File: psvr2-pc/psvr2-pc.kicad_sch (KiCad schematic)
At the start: 89 parts, among them IC1 SN65MLVD200D, IC2 SN65MLVD200D, J1 USB_C_Receptacle, J2 USB3_B_Micro, J3 DP_47272, J4 Barrel_Jack_Switch, J5 Conn_01x02_Pin, Q1 IRF4905, Q2 PN2222A, Q3 IRF9530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

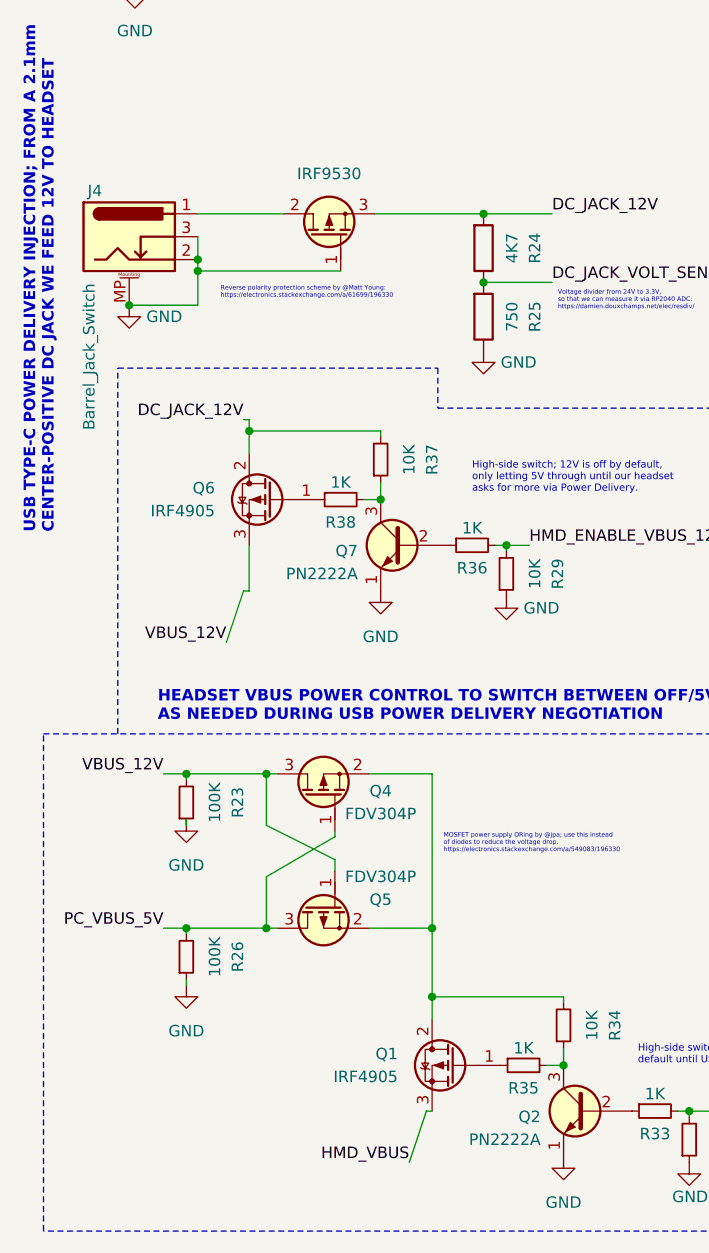
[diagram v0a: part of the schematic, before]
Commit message: Change all the P MOSFETs to Si2301CDS_1_1, and use the correct SOT-23 footprint.
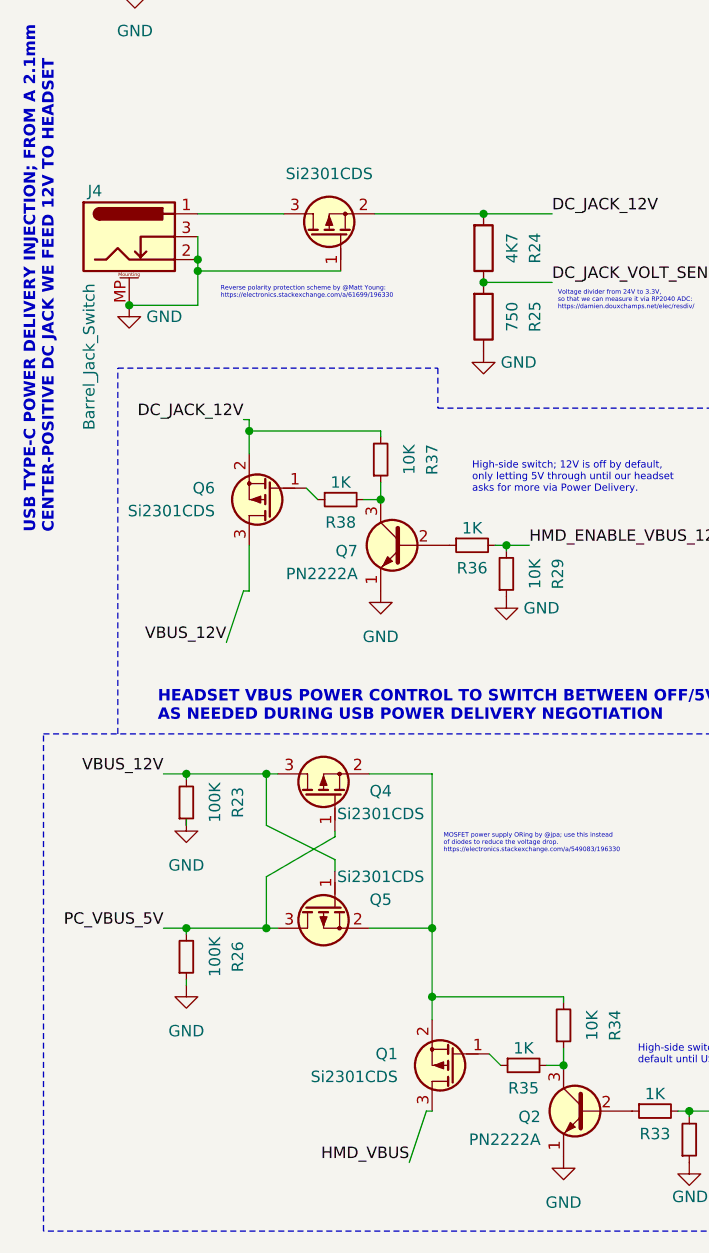
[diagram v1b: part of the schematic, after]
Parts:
- Q1, Q6: value IRF4905 -> Si2301CDS; footprint Package_TO_SOT_SMD:SOT-223 -> Package_TO_SOT_SMD:SOT-23; symbol Transistor_FET:IRF4905 -> PCM_Transistor_MOSFET_AKL:Si2301CDS
- Q2, Q7: footprint Package_TO_SOT_SMD:SOT-223 -> Package_TO_SOT_SMD:SOT-23
- Q3: value IRF9530 -> Si2301CDS; footprint Package_TO_SOT_SMD:SOT-223 -> Package_TO_SOT_SMD:SOT-23; symbol PCM_Transistor_MOSFET_AKL:IRF9530 -> PCM_Transistor_MOSFET_AKL:Si2301CDS
- Q4, Q5: value FDV304P -> Si2301CDS; footprint Package_TO_SOT_SMD:SOT-223 -> Package_TO_SOT_SMD:SOT-23; symbol PCM_Transistor_MOSFET_AKL:FDV304P -> PCM_Transistor_MOSFET_AKL:Si2301CDS
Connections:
- net DC_JACK_12V: now also Q3.2 (S); no longer Q3.3 (S)
- net at J4.1: now also Q3.3 (D); no longer Q3.2 (D)
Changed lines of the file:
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@@
     (stroke (width 0) (type default))
   )
+  (wire (pts (xy 66.04 233.045) (xy 64.77 231.775))
+    (stroke (width 0) (type default))
+  )
   (wire (pts (xy 41.91 33.02) (xy 43.18 33.02))
     (stroke (width 0) (type default))
@@
     (stroke (width 0) (type default))
   )
+  (wire (pts (xy 44.45 168.91) (xy 45.72 170.18))
+    (stroke (width 0) (type default))
+  )
   (wire (pts (xy 194.31 217.17) (xy 192.405 219.075))
     (stroke (width 0) (type default))
@@
     )
   )
-  (symbol (lib_id "PCM_Transistor_MOSFET_AKL:FDV304P") (at 46.355 203.2 270) (mirror x) (unit 1)
+  (symbol (lib_id "PCM_Transistor_MOSFET_AKL:Si2301CDS") (at 46.355 203.2 270) (mirror x) (unit 1)
     (in_bom yes) (on_board yes) (dnp no)
     (property "Reference" "Q4" (at 52.705 202.565 90)
       (effects (font (size 1.27 1.27)))
     )
-    (property "Value" "FDV304P" (at 52.705 205.105 90)
+    (property "Value" "Si2301CDS" (at 52.705 205.105 90)
       (effects (font (size 1.27 1.27)))
     )
-    (property "Footprint" "Package_TO_SOT_SMD:SOT-223" (at 43.815 198.12 0)
+    (property "Footprint" "Package_TO_SOT_SMD:SOT-23" (at 43.815 198.12 0)
       (effects (font (size 1.27 1.27)) hide)
     )
-    (property "Datasheet" "https://www.tme.eu/Document/ac19ef9dcb7c8350177895b6b37394d9/FDV304P.pdf" (at 46.355 203.2 0)
+    (property "Datasheet" "https://www.tme.eu/Document/519498819e90b407235adccdceba4014/SI2301CDS-T1-GE3.pdf" (at 46.355 203.2 0)
       (effects (font (size 1.27 1.27)) hide)
     )
@@
     )
   )
-  (symbol (lib_id "Transistor_FET:IRF4905") (at 60.96 233.045 0) (mirror y) (unit 1)
+  (symbol (lib_id "PCM_Transistor_MOSFET_AKL:Si2301CDS") (at 60.96 233.045 0) (mirror y) (unit 1)
     (in_bom yes) (on_board yes) (dnp no) (fields_autoplaced)
     (property "Reference" "Q1" (at 54.61 231.775 0)
       (effects (font (size 1.27 1.27)) (justify left))
     )
-    (property "Value" "IRF4905" (at 54.61 234.315 0)
+    (property "Value" "Si2301CDS" (at 54.61 234.315 0)
       (effects (font (size 1.27 1.27)) (justify left))
     )
-    (property "Footprint" "Package_TO_SOT_SMD:SOT-223" (at 55.88 234.95 0)
-      (effects (font (size 1.27 1.27) italic) (justify left) hide)
+    (property "Footprint" "Package_TO_SOT_SMD:SOT-23" (at 55.88 235.585 0)
+      (effects (font (size 1.27 1.27)) hide)
     )
-    (property "Datasheet" "http://www.infineon.com/dgdl/irf4905.pdf?fileId=5546d462533600a4015355e32165197c" (at 55.88 236.855 0)
-      (effects (font (size 1.27 1.27)) (justify left) hide)
+    (property "Datasheet" "https://www.tme.eu/Document/519498819e90b407235adccdceba4014/SI2301CDS-T1-GE3.pdf" (at 60.96 233.045 0)
+      (effects (font (size 1.27 1.27)) hide)
     )
     (pin "2")
@@
     )
   )
-  (symbol (lib_id "PCM_Transistor_MOSFET_AKL:IRF9530") (at 46.99 140.97 270) (mirror x) (unit 1)
+  (symbol (lib_id "PCM_Transistor_MOSFET_AKL:Si2301CDS") (at 46.99 140.97 270) (mirror x) (unit 1)
     (in_bom yes) (on_board yes) (dnp no)
     (property "Reference" "Q3" (at 46.99 131.445 90)
       (effects (font (size 1.27 1.27)) hide)
     )
-    (property "Value" "IRF9530" (at 46.99 133.985 90)
+    (property "Value" "Si2301CDS" (at 46.99 133.985 90)
       (effects (font (size 1.27 1.27)))
     )
-    (property "Footprint" "Package_TO_SOT_SMD:SOT-223" (at 44.45 135.89 0)
+    (property "Footprint" "Package_TO_SOT_SMD:SOT-23" (at 44.45 135.89 0)
       (effects (font (size 1.27 1.27)) hide)
     )
-    (property "Datasheet" "https://www.tme.eu/Document/335a97806515fd5b19419c5cf112a667/irf9530.pdf" (at 46.99 140.97 0)
+    (property "Datasheet" "https://www.tme.eu/Document/519498819e90b407235adccdceba4014/SI2301CDS-T1-GE3.pdf" (at 46.99 140.97 0)
       (effects (font (size 1.27 1.27)) hide)
     )
@@
       (effects (font (size 1.27 1.27)) (justify left))
     )
-    (property "Footprint" "Package_TO_SOT_SMD:SOT-223" (at 50.165 172.72 0)
+    (property "Footprint" "Package_TO_SOT_SMD:SOT-23" (at 50.165 172.72 0)
       (effects (font (size 1.27 1.27)) hide)
     )
@@
     )
   )
-  (symbol (lib_id "Transistor_FET:IRF4905") (at 40.64 170.18 0) (mirror y) (unit 1)
+  (symbol (lib_id "PCM_Transistor_MOSFET_AKL:Si2301CDS") (at 40.64 170.18 0) (mirror y) (unit 1)
     (in_bom yes) (on_board yes) (dnp no) (fields_autoplaced)
     (property "Reference" "Q6" (at 34.29 168.91 0)
       (effects (font (size 1.27 1.27)) (justify left))
     )
-    (property "Value" "IRF4905" (at 34.29 171.45 0)
+    (property "Value" "Si2301CDS" (at 34.29 171.45 0)
       (effects (font (size 1.27 1.27)) (justify left))
     )
-    (property "Footprint" "Package_TO_SOT_SMD:SOT-223" (at 35.56 172.085 0)
-      (effects (font (size 1.27 1.27) italic) (justify left) hide)
+    (property "Footprint" "Package_TO_SOT_SMD:SOT-23" (at 35.56 172.72 0)
+      (effects (font (size 1.27 1.27)) hide)
     )
-    (property "Datasheet" "http://www.infineon.com/dgdl/irf4905.pdf?fileId=5546d462533600a4015355e32165197c" (at 35.56 173.99 0)
-      (effects (font (size 1.27 1.27)) (justify left) hide)
+    (property "Datasheet" "https://www.tme.eu/Document/519498819e90b407235adccdceba4014/SI2301CDS-T1-GE3.pdf" (at 40.64 170.18 0)
+      (effects (font (size 1.27 1.27)) hide)
     )
     (pin "2")
@@
       (effects (font (size 1.27 1.27)) (justify left))
     )
-    (property "Footprint" "Package_TO_SOT_SMD:SOT-223" (at 70.485 235.585 0)
+    (property "Footprint" "Package_TO_SOT_SMD:SOT-23" (at 70.485 235.585 0)
       (effects (font (size 1.27 1.27)) hide)
     )
@@
     )
   )
-  (symbol (lib_id "PCM_Transistor_MOSFET_AKL:FDV304P") (at 46.355 215.265 270) (unit 1)
+  (symbol (lib_id "PCM_Transistor_MOSFET_AKL:Si2301CDS") (at 46.355 215.265 270) (unit 1)
     (in_bom yes) (on_board yes) (dnp no)
     (property "Reference" "Q5" (at 52.705 214.63 90)
       (effects (font (size 1.27 1.27)))
     )
-    (property "Value" "FDV304P" (at 52.705 212.09 90)
+    (property "Value" "Si2301CDS" (at 52.705 212.09 90)
       (effects (font (size 1.27 1.27)))
     )
-    (property "Footprint" "Package_TO_SOT_SMD:SOT-223" (at 43.815 220.345 0)
+    (property "Footprint" "Package_TO_SOT_SMD:SOT-23" (at 43.815 220.345 0)
       (effects (font (size 1.27 1.27)) hide)
     )
-    (property "Datasheet" "https://www.tme.eu/Document/ac19ef9dcb7c8350177895b6b37394d9/FDV304P.pdf" (at 46.355 215.265 0)
+    (property "Datasheet" "https://www.tme.eu/Document/519498819e90b407235adccdceba4014/SI2301CDS-T1-GE3.pdf" (at 46.355 215.265 0)
       (effects (font (size 1.27 1.27)) hide)
     )

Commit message: Use a more normal pinheader hole for the SWD stuff/debugging pins for the RP2040 microcontroller. Make it not part of the buyable parts/optional.
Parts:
- J5: footprint Connector:Banana_Jack_2Pin -> Connector_PinHeader_1.00mm:PinHeader_1x02_P1.00mm_Vertical; now left out of the parts list
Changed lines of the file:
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@@
   )
   (symbol (lib_id "Connector:Conn_01x02_Pin") (at 208.915 205.105 270) (mirror x) (unit 1)
-    (in_bom yes) (on_board yes) (dnp no)
+    (in_bom no) (on_board yes) (dnp no)
     (property "Reference" "J5" (at 205.74 208.915 90)
       (effects (font (size 1.27 1.27)) (justify left))
@@
       (effects (font (size 1.27 1.27)) (justify left))
     )
-    (property "Footprint" "Connector:Banana_Jack_2Pin" (at 208.915 205.105 0)
+    (property "Footprint" "Connector_PinHeader_1.00mm:PinHeader_1x02_P1.00mm_Vertical" (at 208.915 205.105 0)
       (effects (font (size 1.27 1.27)) hide)
     )

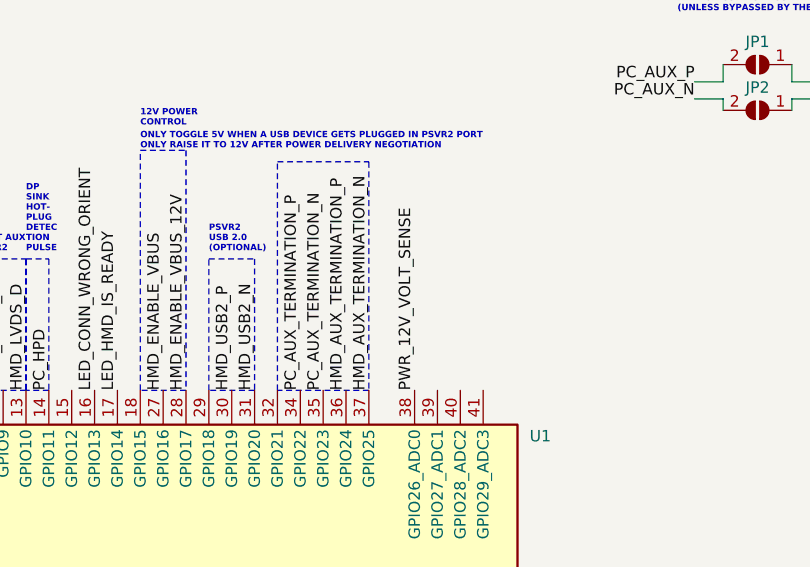
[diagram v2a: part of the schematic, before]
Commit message: Start routing things like power. And more tentative GPIO.
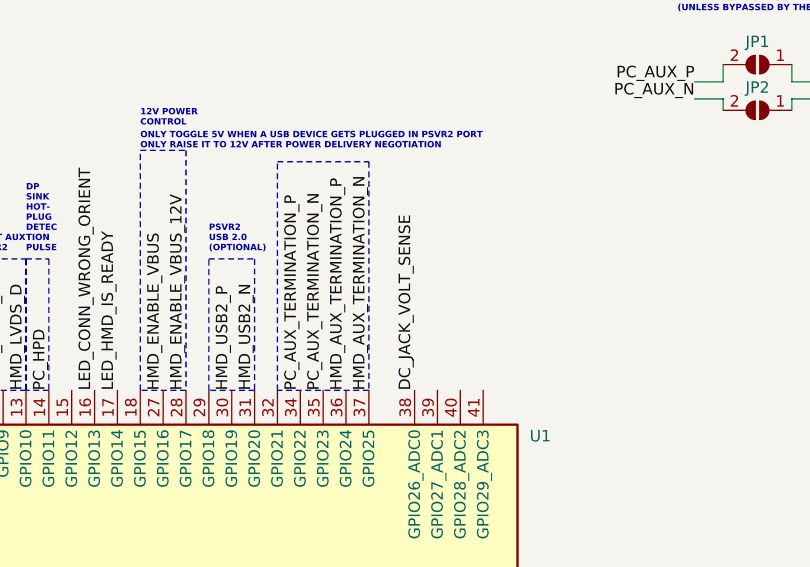
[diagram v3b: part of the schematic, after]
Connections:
- net PWR_12V_VOLT_SENSE is gone; now on net DC_JACK_VOLT_SENSE: U1.38 (GPIO26_ADC0)
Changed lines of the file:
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@@
     (effects (font (size 1.27 1.27)) (justify right bottom))
   )
-  (label "PWR_12V_VOLT_SENSE" (at 208.915 149.225 90) (fields_autoplaced)
+  (label "DC_JACK_VOLT_SENSE" (at 208.915 149.225 90) (fields_autoplaced)
     (effects (font (size 1.27 1.27)) (justify left bottom))
   )

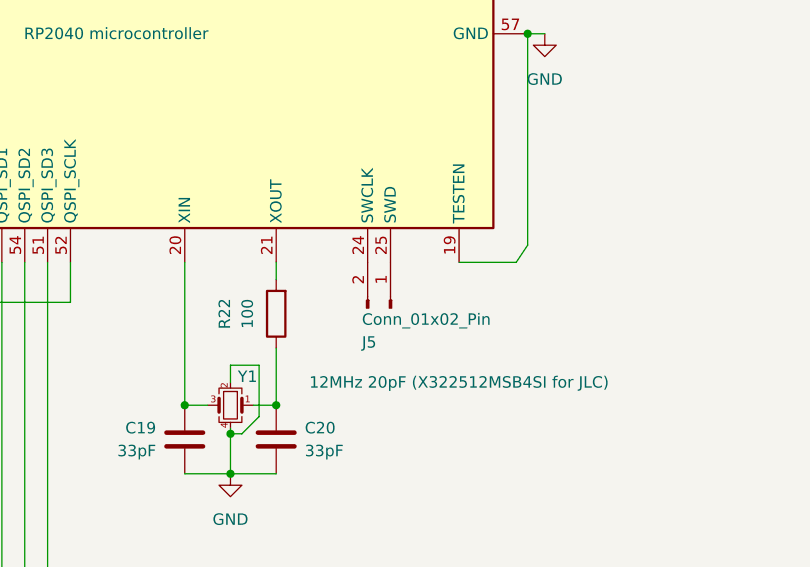
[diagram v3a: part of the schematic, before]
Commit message: Make the SWD pin header have another pin for ground. Reduce the DRC error count a bit more, add more track leeway, reduce polygon overlaps and add missing connections, mainly 3V3 power.
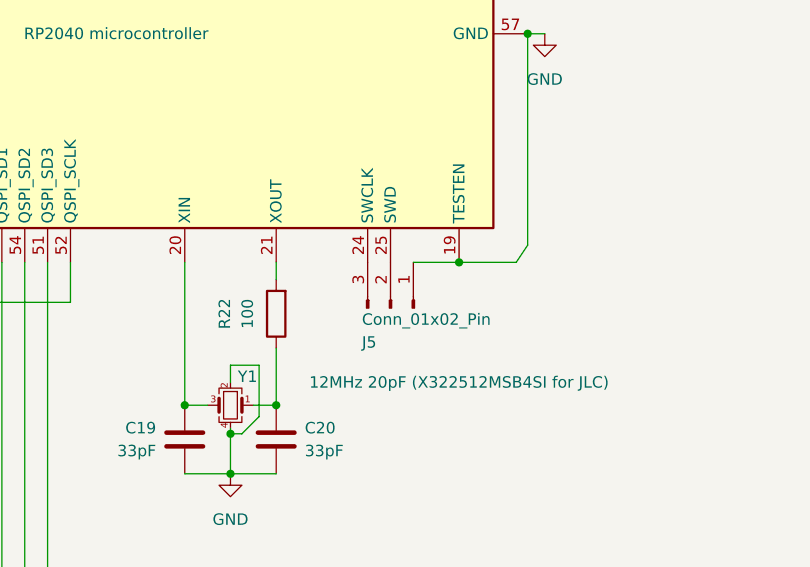
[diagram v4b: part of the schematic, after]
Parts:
- J5: footprint Connector_PinHeader_1.00mm:PinHeader_1x02_P1.00mm_Vertical -> Connector_PinHeader_1.00mm:PinHeader_1x03_P1.00mm_Vertical; symbol Connector:Conn_01x02_Pin -> Connector:Conn_01x03_Pin; now in the parts list
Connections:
- net GND: now also J5.1 (Pin_1)
- net at U1.25 (SWD): now also J5.2 (Pin_2); no longer J5.1 (Pin_1)
- net at U1.24 (SWCLK): now also J5.3 (Pin_3); no longer J5.2 (Pin_2)
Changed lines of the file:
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@@
   (junction (at 297.18 153.67) (diameter 0) (color 0 0 0 0)
   )
+  (junction (at 216.535 200.025) (diameter 0) (color 0 0 0 0)
+  )
   (junction (at 320.675 146.05) (diameter 0) (color 0 0 0 0)
   )
@@
     (stroke (width 0) (type default))
   )
+  (wire (pts (xy 211.455 200.025) (xy 216.535 200.025))
+    (stroke (width 0) (type default))
+  )
   (wire (pts (xy 374.015 23.495) (xy 377.19 23.495))
     (stroke (width 0) (type default))
@@
     )
   )
-  (symbol (lib_id "Connector:Conn_01x02_Pin") (at 208.915 205.105 270) (mirror x) (unit 1)
-    (in_bom no) (on_board yes) (dnp no)
+  (symbol (lib_id "Connector:Conn_01x03_Pin") (at 208.915 205.105 270) (mirror x) (unit 1)
+    (in_bom yes) (on_board yes) (dnp no)
     (property "Reference" "J5" (at 205.74 208.915 90)
       (effects (font (size 1.27 1.27)) (justify left))
@@
       (effects (font (size 1.27 1.27)) (justify left))
     )
-    (property "Footprint" "Connector_PinHeader_1.00mm:PinHeader_1x02_P1.00mm_Vertical" (at 208.915 205.105 0)
+    (property "Footprint" "Connector_PinHeader_1.00mm:PinHeader_1x03_P1.00mm_Vertical" (at 208.915 205.105 0)
       (effects (font (size 1.27 1.27)) hide)
     )
@@
     (pin "1")
     (pin "2")
+    (pin "3")
     (instances
       (project "psvr2-pc"

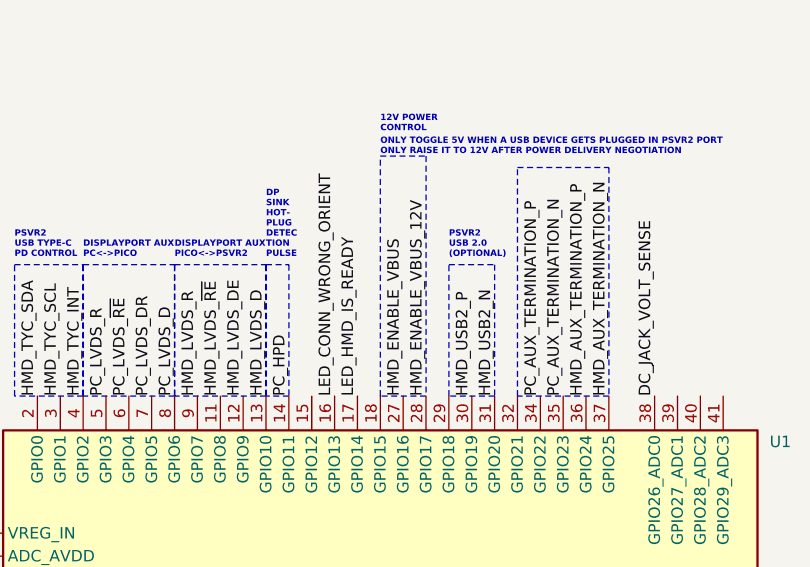
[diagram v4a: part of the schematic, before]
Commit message: Swap to GPIOs to make routing slightly less messy. Make the Open Source Hardware logo line up with the 12V track. Other extra circuiting.
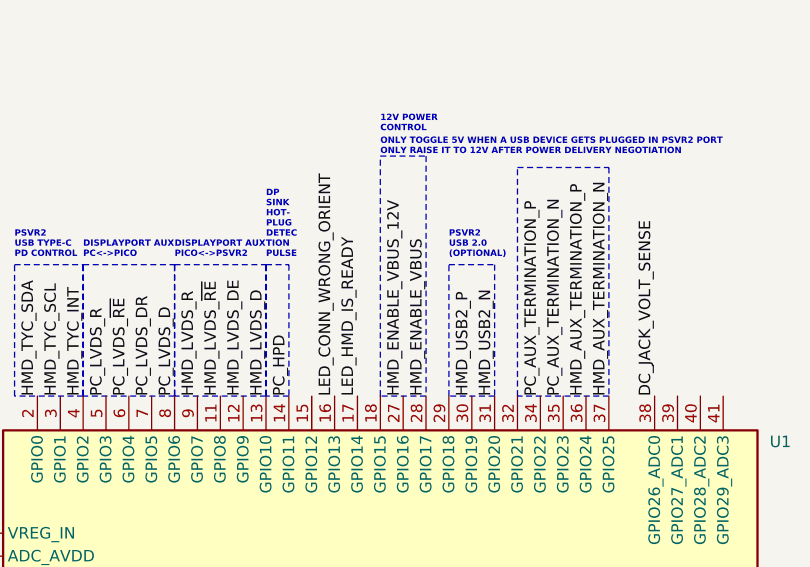
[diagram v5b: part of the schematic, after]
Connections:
- net HMD_ENABLE_VBUS: now also U1.28 (GPIO17); no longer U1.27 (GPIO16)
- net HMD_ENABLE_VBUS_12V: now also U1.27 (GPIO16); no longer U1.28 (GPIO17)
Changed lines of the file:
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@@
     (effects (font (size 1.27 1.27)) (justify right bottom))
   )
-  (label "HMD_ENABLE_VBUS_12V" (at 183.515 149.225 90) (fields_autoplaced)
+  (label "HMD_ENABLE_VBUS" (at 183.515 149.225 90) (fields_autoplaced)
     (effects (font (size 1.27 1.27)) (justify left bottom))
   )
@@
     (effects (font (size 1.27 1.27)) (justify right bottom))
   )
-  (label "HMD_ENABLE_VBUS" (at 180.975 149.225 90) (fields_autoplaced)
+  (label "HMD_ENABLE_VBUS_12V" (at 180.975 149.225 90) (fields_autoplaced)
     (effects (font (size 1.27 1.27)) (justify left bottom))
   )
